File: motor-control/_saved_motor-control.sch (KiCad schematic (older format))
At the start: 17 parts

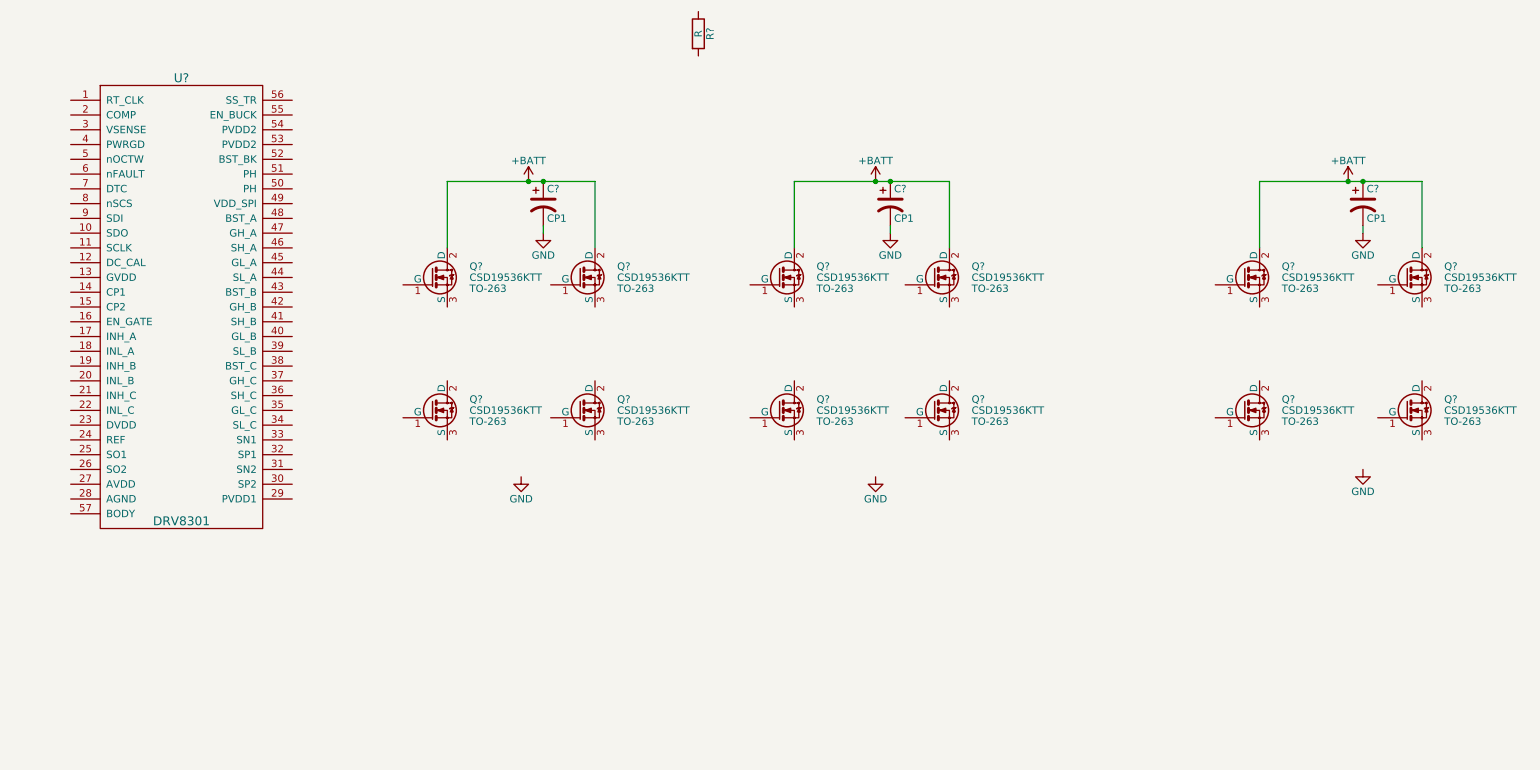
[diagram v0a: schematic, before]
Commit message: added mosfets sheet, & driver sheet
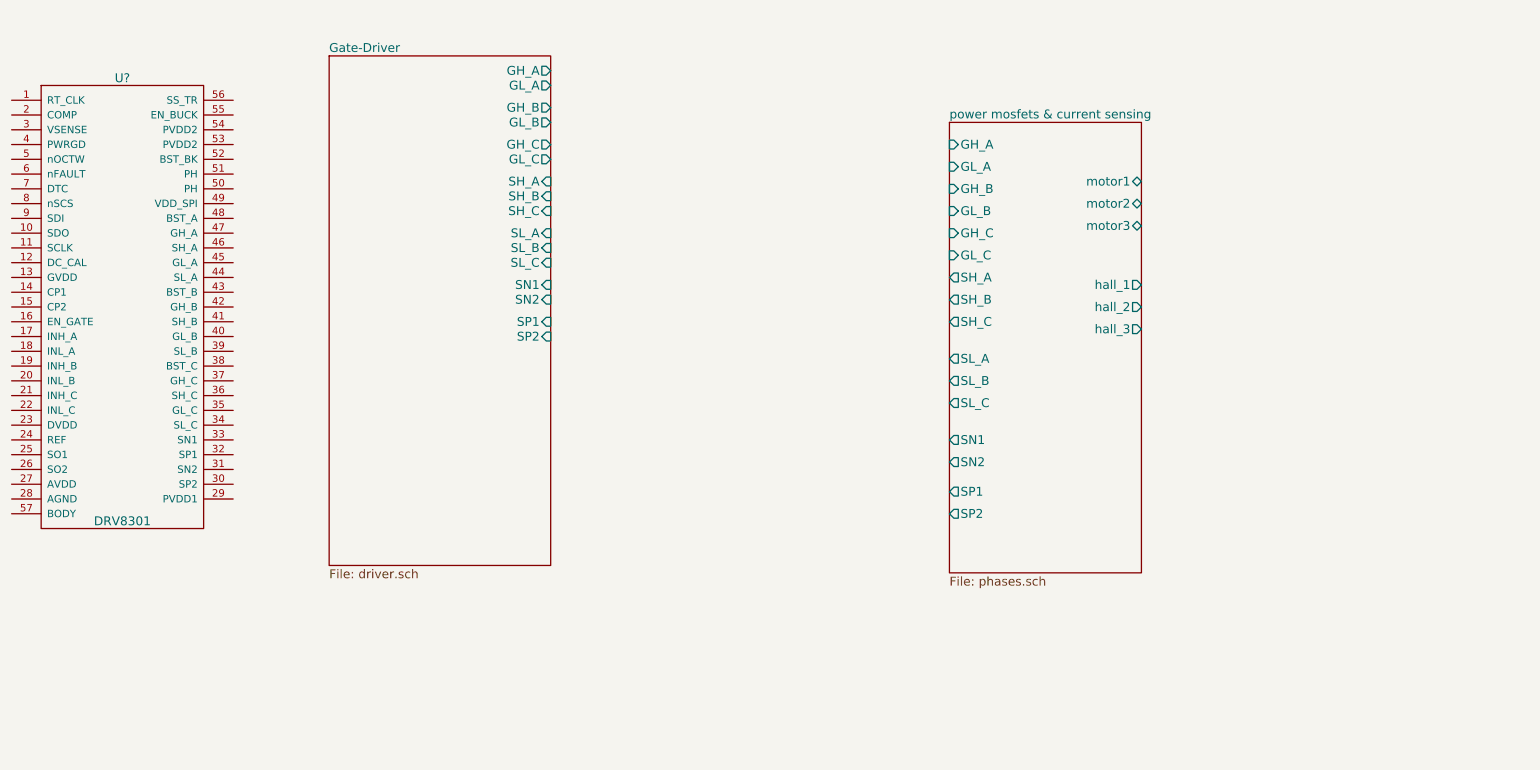
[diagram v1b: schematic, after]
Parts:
- removed C? (x3): CP1, symbol CP1
- removed Q? (x12): CSD19536KTT, TO-263, symbol CSD19536KTT
- removed R?: R, symbol R
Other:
- moved on the sheet: U?

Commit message: Almost finished gate driver schematic
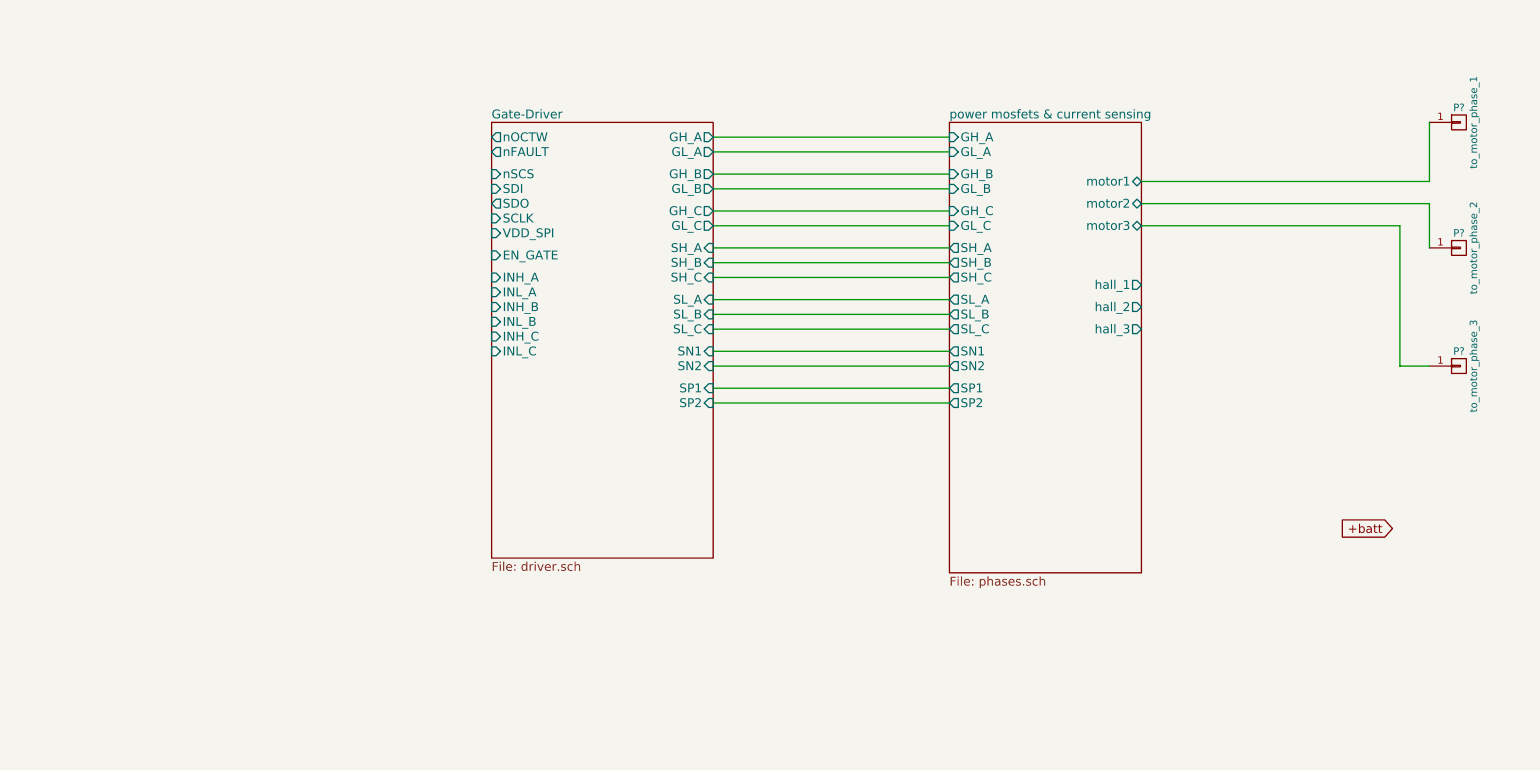
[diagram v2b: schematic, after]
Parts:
- removed U?: DRV8301, symbol DRV8301
- added P?: to_motor_phase_1, symbol CONN_01X01
- added P?: to_motor_phase_2, symbol CONN_01X01
- added P?: to_motor_phase_3, symbol CONN_01X01
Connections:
- net power mosfets & current sensing/motor1: now also P?.1 (P1)
- net power mosfets & current sensing/motor2: now also P?.1 (P1)
- net power mosfets & current sensing/motor3: now also P?.1 (P1)
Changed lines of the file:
@@
 encoding utf-8
 Sheet 1 3
-Title ""
-Date ""
-Rev ""
-Comp ""
-Comment1 ""
+Title "P16261 Motor Controller Schematic -- Top Level"
+Date "2015-11-18"
+Rev "1"
+Comp "RIT Senior Design"
+Comment1 "Joseph Kubeck"
 Comment2 ""
 Comment3 ""
 Comment4 ""
 $EndDescr
-$Comp
-L DRV8301 U?
-U 1 1 5633A2B1
-P 1700 3000
-F 0 "U?" H 1700 4150 60  0000 C CNN
-F 1 "DRV8301" H 1700 1150 60  0000 C CNN
-F 2 "" H 1700 3000 60  0000 C CNN
-F 3 "" H 1700 3000 60  0000 C CNN
-	1    1700 3000
-	1    0    0    -1
-$EndComp
 $Sheet
 S 7300 2150 1300 3050
@@
 F0 "power mosfets & current sensing" 60
 F1 "phases.sch" 60
-F2 "GH_A" I L 7300 2300 60
-F3 "GL_A" I L 7300 2450 60
-F4 "GH_B" I L 7300 2600 60
-F5 "GL_B" I L 7300 2750 60
-F6 "GH_C" I L 7300 2900 60
-F7 "GL_C" I L 7300 3050 60
+F2 "GH_A" I L 7300 2250 60
+F3 "GL_A" I L 7300 2350 60
+F4 "GH_B" I L 7300 2500 60
+F5 "GL_B" I L 7300 2600 60
+F6 "GH_C" I L 7300 2750 60
+F7 "GL_C" I L 7300 2850 60
 F8 "motor2" B R 8600 2700 60
 F9 "motor1" B R 8600 2550 60
 F10 "motor3" B R 8600 2850 60
-F11 "SH_A" O L 7300 3200 60
-F12 "SH_B" O L 7300 3350 60
-F13 "SH_C" O L 7300 3500 60
-F14 "SL_A" O L 7300 3750 60
-F15 "SL_B" O L 7300 3900 60
-F16 "SL_C" O L 7300 4050 60
-F17 "SN1" O L 7300 4300 60
-F18 "SN2" O L 7300 4450 60
-F19 "SP1" O L 7300 4650 60
-F20 "SP2" O L 7300 4800 60
+F11 "SH_A" O L 7300 3000 60
+F12 "SH_B" O L 7300 3100 60
+F13 "SH_C" O L 7300 3200 60
+F14 "SL_A" O L 7300 3350 60
+F15 "SL_B" O L 7300 3450 60
+F16 "SL_C" O L 7300 3550 60
+F17 "SN1" O L 7300 3700 60
+F18 "SN2" O L 7300 3800 60
+F19 "SP1" O L 7300 3950 60
+F20 "SP2" O L 7300 4050 60
 F21 "hall_1" O R 8600 3250 60
 F22 "hall_2" O R 8600 3400 60
@@
 $EndSheet
 $Sheet
-S 3100 1700 1500 3450
+S 4200 2150 1500 2950
 U 56433028
 F0 "Gate-Driver" 60
 F1 "driver.sch" 60
-F2 "GH_A" O R 4600 1800 60
-F3 "GL_A" O R 4600 1900 60
-F4 "GH_B" O R 4600 2050 60
-F5 "GL_B" O R 4600 2150 60
-F6 "GH_C" O R 4600 2300 60
-F7 "GL_C" O R 4600 2400 60
-F8 "SH_A" I R 4600 2550 60
-F9 "SH_B" I R 4600 2650 60
-F10 "SH_C" I R 4600 2750 60
-F11 "SL_A" I R 4600 2900 60
-F12 "SL_B" I R 4600 3000 60
-F13 "SL_C" I R 4600 3100 60
-F14 "SN1" I R 4600 3250 60
-F15 "SN2" I R 4600 3350 60
-F16 "SP1" I R 4600 3500 60
-F17 "SP2" I R 4600 3600 60
+F2 "GH_A" O R 5700 2250 60
+F3 "GL_A" O R 5700 2350 60
+F4 "GH_B" O R 5700 2500 60
+F5 "GL_B" O R 5700 2600 60
+F6 "GH_C" O R 5700 2750 60
+F7 "GL_C" O R 5700 2850 60
+F8 "SH_A" I R 5700 3000 60
+F9 "SH_B" I R 5700 3100 60
+F10 "SH_C" I R 5700 3200 60
+F11 "SL_A" I R 5700 3350 60
+F12 "SL_B" I R 5700 3450 60
+F13 "SL_C" I R 5700 3550 60
+F14 "SN1" I R 5700 3700 60
+F15 "SN2" I R 5700 3800 60
+F16 "SP1" I R 5700 3950 60
+F17 "SP2" I R 5700 4050 60
+F18 "nOCTW" O L 4200 2250 60
+F19 "nFAULT" O L 4200 2350 60
+F20 "nSCS" I L 4200 2500 60
+F21 "SDI" I L 4200 2600 60
+F22 "SDO" O L 4200 2700 60
+F23 "SCLK" I L 4200 2800 60
+F24 "EN_GATE" I L 4200 3050 60
+F25 "INH_A" I L 4200 3200 60
+F26 "INL_A" I L 4200 3300 60
+F27 "INH_B" I L 4200 3400 60
+F28 "INL_B" I L 4200 3500 60
+F29 "INH_C" I L 4200 3600 60
+F30 "INL_C" I L 4200 3700 60
+F31 "VDD_SPI" I L 4200 2900 60
 $EndSheet
+$Comp
+L CONN_01X01 P?
+U 1 1 5643889D
+P 10750 2150
+F 0 "P?" H 10750 2250 50  0000 C CNN
+F 1 "to_motor_phase_1" V 10850 2150 50  0000 C CNN
+F 2 "" H 10750 2150 60  0000 C CNN
+F 3 "" H 10750 2150 60  0000 C CNN
+	1    10750 2150
+	1    0    0    -1
+$EndComp
+$Comp
+L CONN_01X01 P?
+U 1 1 56438B24
+P 10750 3000
+F 0 "P?" H 10750 3100 50  0000 C CNN
+F 1 "to_motor_phase_2" V 10850 3000 50  0000 C CNN
+F 2 "" H 10750 3000 60  0000 C CNN
+F 3 "" H 10750 3000 60  0000 C CNN
+	1    10750 3000
+	1    0    0    -1
+$EndComp
+$Comp
+L CONN_01X01 P?
+U 1 1 56438C23
+P 10750 3800
+F 0 "P?" H 10750 3900 50  0000 C CNN
+F 1 "to_motor_phase_3" V 10850 3800 50  0000 C CNN
+F 2 "" H 10750 3800 60  0000 C CNN
+F 3 "" H 10750 3800 60  0000 C CNN
+	1    10750 3800
+	1    0    0    -1
+$EndComp
+Wire Wire Line
+	8600 2550 10550 2550
+Wire Wire Line
+	10550 2550 10550 2150
+Wire Wire Line
+	8600 2700 10550 2700
+Wire Wire Line
+	10550 2700 10550 3000
+Wire Wire Line
+	8600 2850 10350 2850
+Wire Wire Line
+	10350 2850 10350 3800
+Wire Wire Line
+	10350 3800 10550 3800
+Wire Wire Line
+	5700 2250 7300 2250
+Wire Wire Line
+	5700 2350 7300 2350
+Wire Wire Line
+	5700 2500 7300 2500
+Wire Wire Line
+	5700 2600 7300 2600
+Wire Wire Line
+	5700 2750 7300 2750
+Wire Wire Line
+	5700 2850 7300 2850
+Wire Wire Line
+	5700 3000 7300 3000
+Wire Wire Line
+	5700 3100 7300 3100
+Wire Wire Line
+	5700 3200 7300 3200
+Wire Wire Line
+	5700 3350 7300 3350
+Wire Wire Line
+	5700 3450 7300 3450
+Wire Wire Line
+	5700 3550 7300 3550
+Wire Wire Line
+	5700 3700 7300 3700
+Wire Wire Line
+	5700 3800 7300 3800
+Wire Wire Line
+	5700 3950 7300 3950
+Wire Wire Line
+	5700 4050 7300 4050
+Text GLabel 10300 4900 0    60   Input ~ 0
++batt
 $EndSCHEMATC

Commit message: Ready for pcb design. Schematic capture seems good
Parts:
- added P?: CONN_02X12, symbol CONN_02X12
- added P? (x2): CONN_01X01, symbol CONN_01X01
- added R? (x2): DNP, symbol R
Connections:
- net +batt: now also P?.1 (P1)
- net Gate-Driver/EN_GATE: now also P?.4 (P4)
- net Gate-Driver/INH_A: now also P?.6 (P6)
- net Gate-Driver/INH_B: now also P?.10 (P10)
- net Gate-Driver/INH_C: now also P?.14 (P14)
- net Gate-Driver/INL_A: now also P?.8 (P8)
- net Gate-Driver/INL_B: now also P?.12 (P12)
- net Gate-Driver/INL_C: now also P?.16 (P16)
- net Gate-Driver/SCLK: now also P?.1 (P1)
- net Gate-Driver/SDI: now also P?.5 (P5)
- net Gate-Driver/SDO: now also P?.3 (P3)
- net Gate-Driver/SN2: now also R?.1
- net Gate-Driver/SP2: now also R?.1
- net Gate-Driver/VDD_SPI: now also P?.2 (P2)
- net Gate-Driver/nFAULT: now also P?.9 (P9)
- net Gate-Driver/nOCTW: now also P?.11 (P11)
- net Gate-Driver/nSCS: now also P?.7 (P7)
- net power mosfets & current sensing/hall_1: now also P?.19 (P19)
- net power mosfets & current sensing/hall_2: now also P?.21 (P21)
- net power mosfets & current sensing/hall_3: now also P?.23 (P23)
- new net GND: P?.1 (P1)
- new net Gate-Driver/DC_CAL: P?.18 (P18)
- new net Gate-Driver/REF: P?.20 (P20)
- new net Gate-Driver/S01: P?.22 (P22)
- new net Gate-Driver/S02: P?.24 (P24)
- new net power mosfets & current sensing/SN3: R?.2
- new net power mosfets & current sensing/SP3: R?.2
